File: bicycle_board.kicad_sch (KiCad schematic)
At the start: 59 parts, among them J1 Conn_02x05_Odd_Even, J10 USB_A, J12 Conn_01x04, J13 Conn_01x04, J2 USB_C_Receptacle_USB2.0_16P, J5 Micro_SD_Card, J6 Conn_01x08, J7 Conn_01x03, J8 Conn_01x02, J9 Conn_01x06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

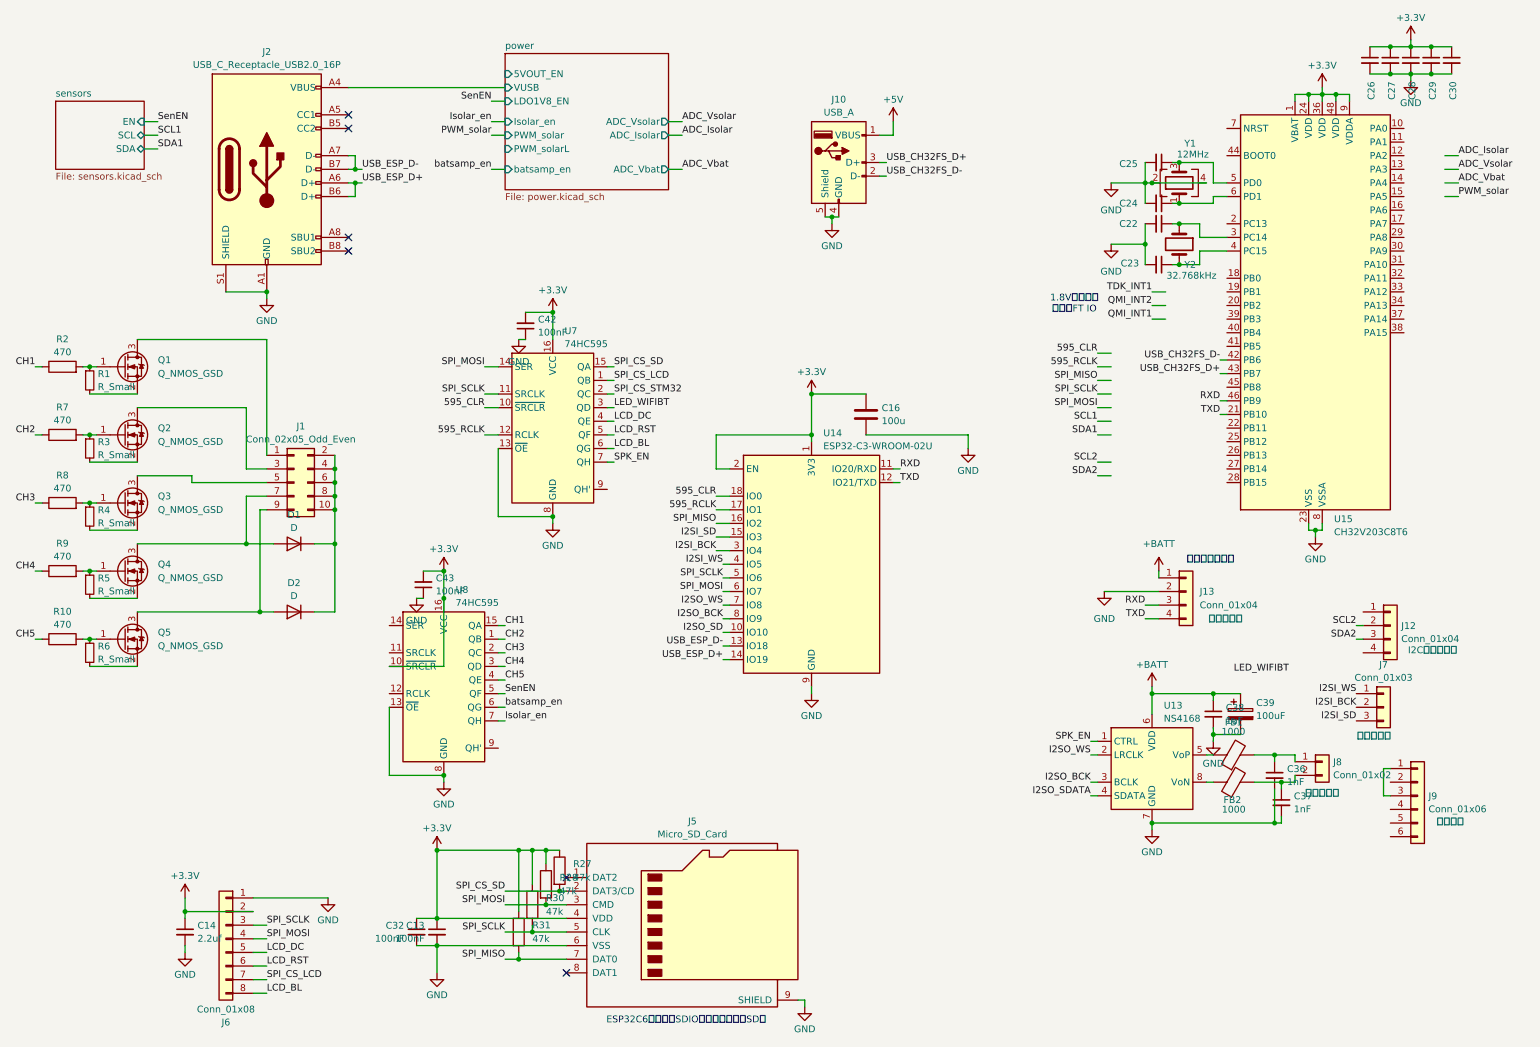
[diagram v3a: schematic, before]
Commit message: 收窄PCB宽度到47.4mm
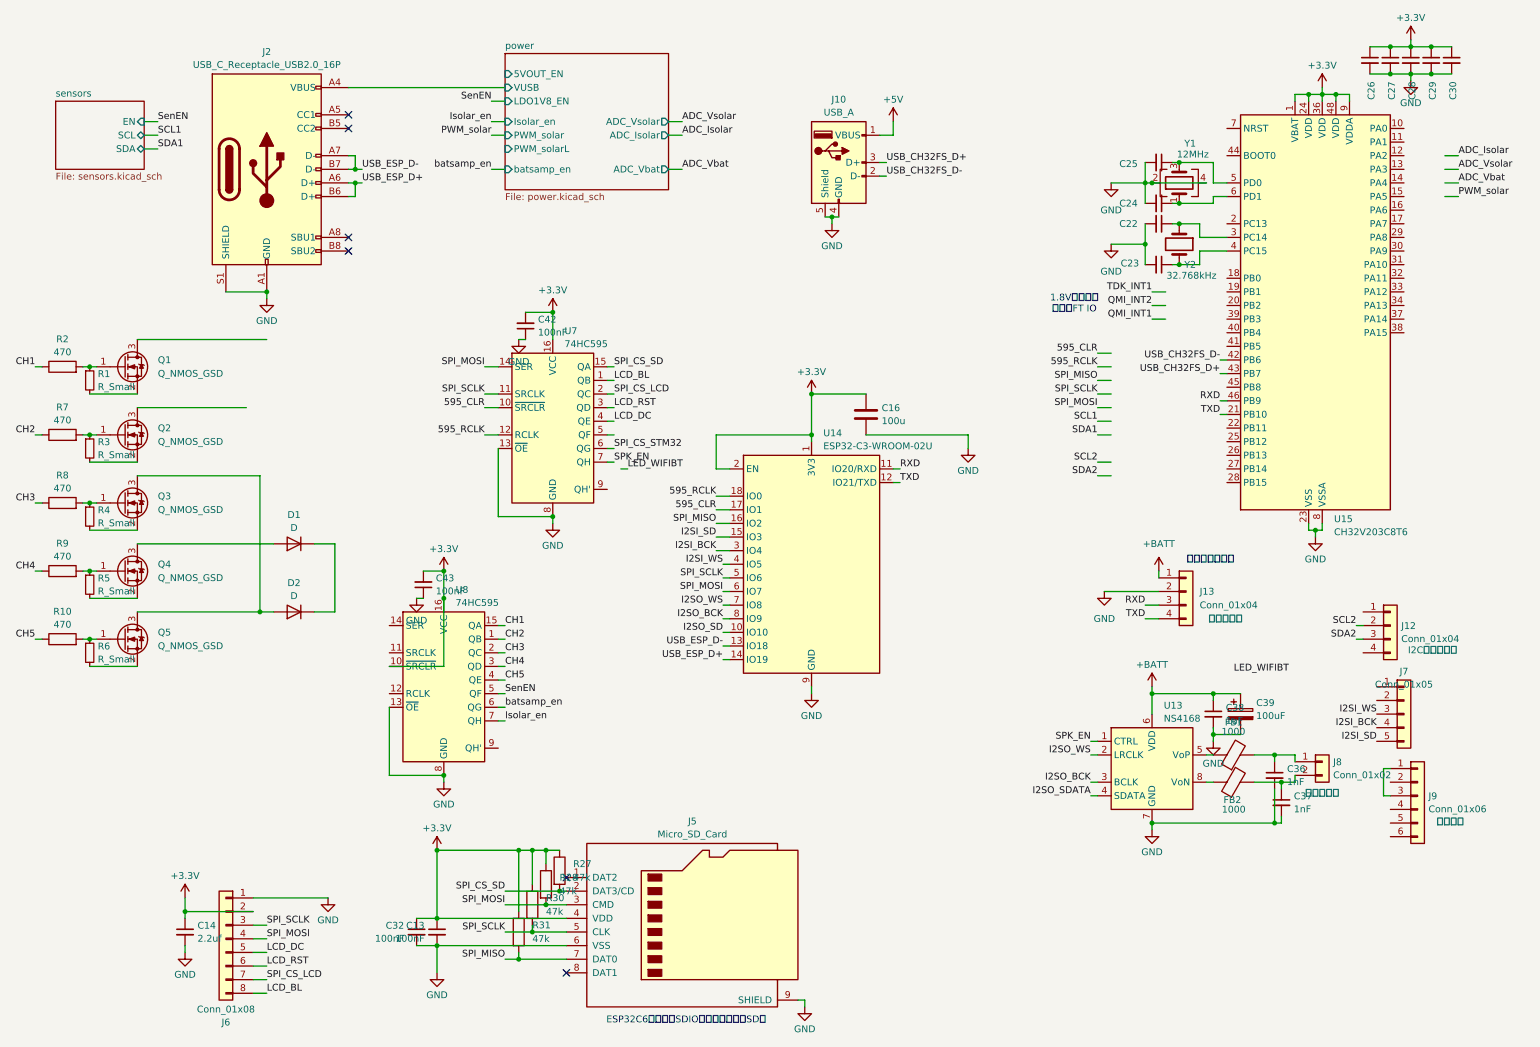
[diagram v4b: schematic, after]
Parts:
- removed J1: Conn_02x05_Odd_Even, Connector_PinSocket_2.54mm:PinSocket_2x05_P2.54mm_Vertical, symbol Connector_Generic:Conn_02x05_Odd_Even
- removed J7: Conn_01x03, Connector_PinHeader_2.54mm:PinHeader_1x03_P2.54mm_Vertical, symbol Connector_Generic:Conn_01x03
- added J7: Conn_01x05, Connector_JST:JST_GH_BM05B-GHS-TBT_1x05-1MP_P1.25mm_Vertical, symbol Connector_Generic:Conn_01x05
- J12: footprint Connector_PinHeader_2.54mm:PinHeader_1x04_P2.54mm_Vertical -> Connector_JST:JST_GH_BM04B-GHS-TBT_1x04-1MP_P1.25mm_Vertical
- J6: footprint Connector_PinHeader_2.54mm:PinHeader_1x08_P2.54mm_Vertical -> Connector_JST:JST_GH_BM08B-GHS-TBT_1x08-1MP_P1.25mm_Vertical
- J9: footprint Connector_PinSocket_1.27mm:PinSocket_1x06_P1.27mm_Vertical -> Connector_JST:JST_SHL_SM06B-SHLS-TF_1x06-1MP_P1.00mm_Horizontal
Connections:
- net 595_CLR: now also U14.17 (IO1); no longer U14.18 (IO0)
- net 595_RCLK: now also U14.18 (IO0); no longer U14.17 (IO1)
- net I2SI_BCK: now also J7.4 (Pin_4)
- net I2SI_SD: now also J7.5 (Pin_5)
- net I2SI_WS: now also J7.3 (Pin_3)
- net LCD_BL: now also U7.1 (QB); no longer U7.6 (QG)
- net LCD_RST: now also U7.3 (QD); no longer U7.5 (QF)
- net LED_WIFIBT: no longer U7.3 (QD)
- net SPI_CS_LCD: now also U7.2 (QC); no longer U7.1 (QB)
- net SPI_CS_STM32: now also U7.6 (QG); no longer U7.2 (QC)
- net at Q3.3 (D): now also D2.2 (A), Q5.3 (D)

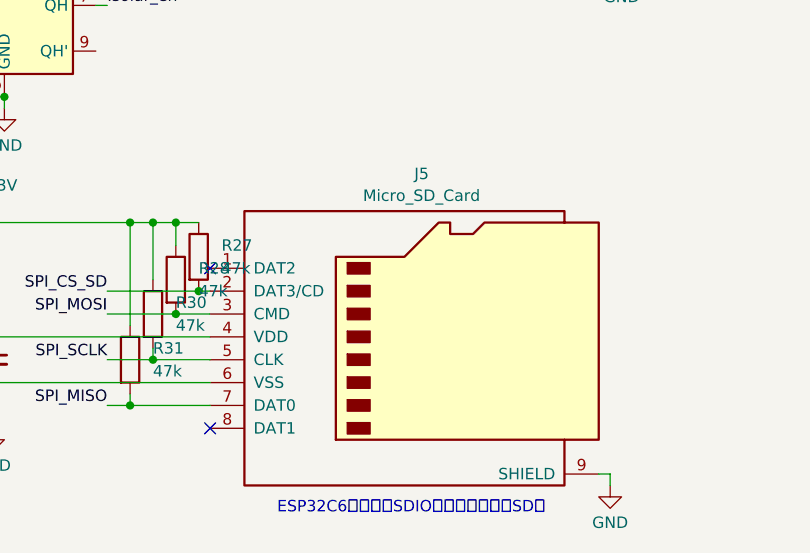
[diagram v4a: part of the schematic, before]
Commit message: 画我现有的SD卡槽封装，应用到PCB
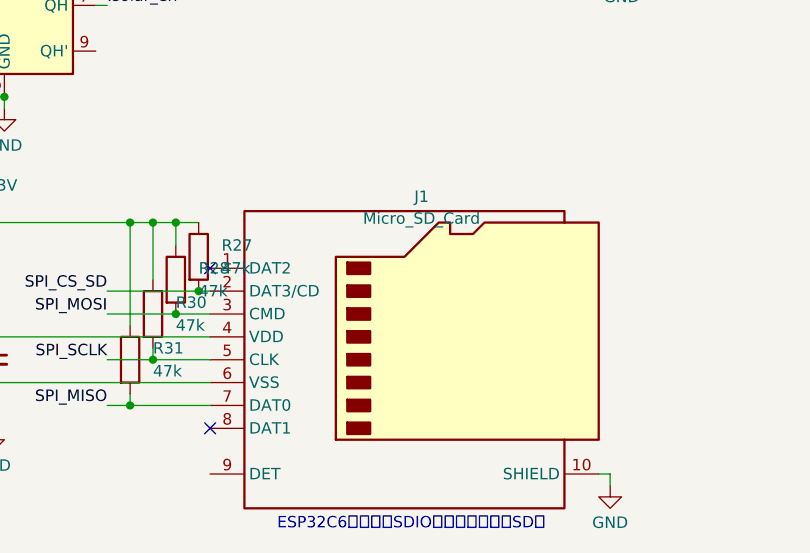
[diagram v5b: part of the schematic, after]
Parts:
- removed J5: Micro_SD_Card, Connector_Card:microSD_HC_Hirose_DM3AT-SF-PEJM5, symbol Connector:Micro_SD_Card
- added J1: Micro_SD_Card, Library:microSD_Slot_mybuy, symbol Connector:Micro_SD_Card_Det1
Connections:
- net +3.3V: now also J1.4 (VDD)
- net GND: now also J1.10 (SHIELD), J1.6 (VSS)
- net SPI_CS_SD: now also J1.2 (DAT3/CD)
- net SPI_MISO: now also J1.7 (DAT0)
- net SPI_MOSI: now also J1.3 (CMD)
- net SPI_SCLK: now also J1.5 (CLK)
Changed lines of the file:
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@@
 	(text "ESP32C6只能作为SDIO从机，无法驱动SD卡"
 		(exclude_from_sim no)
-		(at 140.462 195.58 0)
+		(at 140.462 197.358 0)
 		(effects
 			(font
@@
 	)
 	(symbol
+		(lib_id "Connector:Micro_SD_Card_Det1")
+		(at 140.97 179.07 0)
+		(unit 1)
+		(exclude_from_sim no)
+		(in_bom yes)
+		(on_board yes)
+		(dnp no)
+		(property "Reference" "J1"
+			(at 141.605 160.9555 0)
+			(effects
+				(font
+					(size 1.27 1.27)
+				)
+			)
+		)
+		(property "Value" "Micro_SD_Card"
+			(at 141.605 163.3798 0)
+			(effects
+				(font
+					(size 1.27 1.27)
+				)
+			)
+		)
+		(property "Footprint" "Library:microSD_Slot_mybuy"
+			(at 193.04 161.29 0)
+			(effects
+				(font
+					(size 1.27 1.27)
+				)
+				(hide yes)
+			)
+		)
+		(property "Datasheet" "https://datasheet.lcsc.com/lcsc/2110151630_XKB-Connectivity-XKTF-015-N_C381082.pdf"
+			(at 140.97 176.53 0)
+			(effects
+				(font
+					(size 1.27 1.27)
+				)
+				(hide yes)
+			)
+		)
+		(property "Description" "Micro SD Card Socket with one card detection pin"
+			(at 140.97 179.07 0)
+			(effects
+				(font
+					(size 1.27 1.27)
+				)
+				(hide yes)
+			)
+		)
+		(property "Sim.Type" ""
+			(at 140.97 179.07 0)
+			(effects
+				(font
+					(size 1.27 1.27)
+				)
+				(hide yes)
+			)
+		)
+		(pin "9"
+		)
+		(pin "2"
+		)
+		(pin "4"
+		)
+		(pin "3"
+		)
+		(pin "7"
+		)
+		(pin "1"
+		)
+		(pin "6"
+		)
+		(pin "8"
+		)
+		(pin "5"
+		)
+		(pin "10"
+		)
+		(instances
+			(project "bicycle_board"
+				(path "/a369956d-4c9f-46c3-810f-e3e9616ab1a2"
+					(reference "J1")
+					(unit 1)
+				)
+			)
+		)
+	)
+	(symbol
 		(lib_id "Device:R_Small")
 		(at 29.21 76.2 0)
@@
 					(unit 1)
 				)
-			)
-		)
-	)
-	(symbol
-		(lib_id "Connector:Micro_SD_Card")
-		(at 140.97 176.53 0)
-		(unit 1)
-		(exclude_from_sim no)
-		(in_bom yes)
-		(on_board yes)
-		(dnp no)
-		(property "Reference" "J5"
-			(at 141.605 158.4155 0)
-			(effects
-				(font
-					(size 1.27 1.27)
-				)
-			)
-		)
-		(property "Value" "Micro_SD_Card"
-			(at 141.605 160.8398 0)
-			(effects
-				(font
-					(size 1.27 1.27)
-				)
-			)
-		)
-		(property "Footprint" "Connector_Card:microSD_HC_Hirose_DM3AT-SF-PEJM5"
-			(at 170.18 168.91 0)
-			(effects
-				(font
-					(size 1.27 1.27)
-				)
-				(hide yes)
-			)
-		)
-		(property "Datasheet" "http://katalog.we-online.de/em/datasheet/693072010801.pdf"
-			(at 140.97 176.53 0)
-			(effects
-				(font
-					(size 1.27 1.27)
-				)
-				(hide yes)
-			)
-		)
-		(property "Description" "Micro SD Card Socket"
-			(at 140.97 176.53 0)
-			(effects
-				(font
-					(size 1.27 1.27)
-				)
-				(hide yes)
-			)
-		)
-		(property "Sim.Type" ""
-			(at 140.97 176.53 0)
-			(effects
-				(font
-					(size 1.27 1.27)
-				)
-				(hide yes)
-			)
-		)
-		(pin "9"
-		)
-		(pin "2"
-		)
-		(pin "4"
-		)
-		(pin "3"
-		)
-		(pin "7"
-		)
-		(pin "1"
-		)
-		(pin "6"
-		)
-		(pin "8"
-		)
-		(pin "5"
-		)
-		(instances
-			(project ""
-				(path "/a369956d-4c9f-46c3-810f-e3e9616ab1a2"
-					(reference "J5")
-					(unit 1)
-				)

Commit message: PCB宽度进一步收缩到41.4mm，晶振改2016和2012，最小线距改0.15mm，添加一些布线
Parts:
- Y1: footprint Crystal:Crystal_SMD_3225-4Pin_3.2x2.5mm -> Crystal:Crystal_SMD_2016-4Pin_2.0x1.6mm
- Y2: footprint Crystal:Crystal_SMD_3215-2Pin_3.2x1.5mm -> Crystal:Crystal_SMD_2012-2Pin_2.0x1.2mm
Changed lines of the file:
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@@
 			)
 		)
-		(property "Footprint" "Crystal:Crystal_SMD_3215-2Pin_3.2x1.5mm"
+		(property "Footprint" "Crystal:Crystal_SMD_2012-2Pin_2.0x1.2mm"
 			(at 232.41 50.8 0)
 			(effects
@@
 			)
 		)
-		(property "Footprint" "Crystal:Crystal_SMD_3225-4Pin_3.2x2.5mm"
+		(property "Footprint" "Crystal:Crystal_SMD_2016-4Pin_2.0x1.6mm"
 			(at 232.41 39.37 0)
 			(effects

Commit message: 连接大多数布线，做一些调整，添加覆铜
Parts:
- added C48: 100n, Capacitor_SMD:C_0402_1005Metric, symbol Device:C_Small
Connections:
- net I2SO_SDATA is gone; now on net I2SO_SD: U13.4 (SDATA)
- net +3.3V: now also J12.1 (Pin_1)
- net ADC_Isolar: now also U15.16 (PA6)
- net ADC_Vbat: now also U15.17 (PA7)
- net ADC_Vsolar: now also U15.18 (PB0)
- net GND: now also J12.2 (Pin_2), C48.1
- net I2SI_BCK: no longer U14.3 (IO4)
- net I2SI_SD: no longer U14.15 (IO3)
- net I2SI_WS: no longer U14.4 (IO5)
- net I2SO_BCK: now also U14.7 (IO8); no longer U14.8 (IO9)
- net I2SO_SD: now also U14.4 (IO5); no longer U14.10 (IO10)
- net I2SO_WS: now also U14.8 (IO9); no longer U14.7 (IO8)
- net RXD: now also U15.31 (PA10); no longer U15.46 (PB9)
- net SCL1: now also U15.45 (PB8)
- net SCL2: now also J12.3 (Pin_3), U15.21 (PB10); no longer J12.2 (Pin_2)
- net SDA1: now also U15.46 (PB9)
- net SDA2: now also J12.4 (Pin_4), U15.22 (PB11); no longer J12.3 (Pin_3)
- net SPI_MISO: now also U15.27 (PB14)
- net SPI_MOSI: now also U15.28 (PB15)
- net SPI_SCLK: now also U15.26 (PB13)
- net TXD: now also U15.30 (PA9); no longer U15.21 (PB10)
- net USB_CH32FS_D+: now also U15.33 (PA12); no longer U15.43 (PB7)
- net USB_CH32FS_D-: now also U15.32 (PA11); no longer U15.42 (PB6)
- net SPISen_CS_QMI_3V3: now reaches U15.38 (PA15)
- net SPISen_SCLK_3V3: now reaches U15.39 (PB3)
- net SPISen_MISO_3V3: now reaches U15.40 (PB4)
- net SPISen_MOSI_3V3: now reaches U15.41 (PB5)
- net at U15.7 (NRST): now also C48.2
- new net SPISen_CS_TDK_3V3: U15.42 (PB6)
- new net TDK_INT2_3V3: U15.43 (PB7)
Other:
- sheet sensors ports: added CS_QMI_3V3, CS_TDK_3V3, MISO_3V3, MOSI_3V3, SCLK_3V3, TDK_INT2_3V3; removed none
- moved on the sheet: J10
